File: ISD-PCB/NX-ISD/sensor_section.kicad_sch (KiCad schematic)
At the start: 27 parts, among them U10 BNO085, U11 PCA9306, U12 OPT3001DNPR, U3 MAX17048G_T10, U4 RV-3028-C7, U5 MAX30102, U6 BME690, Y2 32.768

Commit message: v1p3 - Isssues fixed
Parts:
- added R16, R17: 10k, Resistor_SMD:R_0402_1005Metric, symbol Device:R
- Y1: renamed from Y2; value 32.768 -> 32.768 kHz; Capacity (none) -> 12,5pF; ESR (none) -> 70 kOhms; Manufacterer part number (none) -> DH2032K768C5T1521011; Tolerance (none) -> ±20ppm
- renumbered C2 to C12, C1 to C13, C5 to C14, C18 to C15, C4 to C16, C7 to C17, C12 to C18, C30 to C19, C6 to C20, C29 to C21, C28 to C22, C27 to C23, R6 to R10, R23 to R11, R22 to R12, R18 to R13, R19 to R14, R24 to R15, R17 to R18, U12 to U10, U10 to U11, U4 to U12, U3 to U6, U6 to U7, U5 to U8, U11 to U9
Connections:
- net +3V3: now also U8.10 (VLED+), R16.1, R17.1
- net at U11.15 (ENV_SCL): now also R17.2
- net at U11.16 (ENV_SDA): now also R16.2
- no-connect marks 3 -> 1
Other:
- moved on the sheet: R18

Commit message: v1p3 - fixed
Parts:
- C14: value 100n -> 1u; footprint Capacitor_SMD:C_0402_1005Metric -> Capacitor_SMD:C_0603_1608Metric
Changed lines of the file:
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@@
 		)
 	)
+	(text "[0603]"
+		(exclude_from_sim no)
+		(at 31.242 176.53 0)
+		(effects
+			(font
+				(size 1.27 1.27)
+			)
+		)
+	)
 	(junction
 		(at 266.7 63.5)
@@
 		(dnp no)
 		(property "Reference" "C16"
-			(at 86.36 63.246 0)
+			(at 86.868 60.706 0)
 			(show_name no)
 			(do_not_autoplace no)
@@
 		)
 		(property "Value" "1u"
-			(at 86.868 66.04 0)
+			(at 88.138 65.786 0)
 			(show_name no)
 			(do_not_autoplace no)
@@
 		(dnp no)
 		(property "Reference" "C15"
-			(at 44.704 174.498 90)
+			(at 43.18 169.418 0)
 			(show_name no)
 			(do_not_autoplace no)
@@
 		)
 		(property "Value" "100n"
-			(at 51.816 174.752 90)
+			(at 42.926 175.006 0)
 			(show_name no)
 			(do_not_autoplace no)
@@
 		(dnp no)
 		(property "Reference" "C14"
-			(at 34.544 174.498 90)
+			(at 33.528 169.672 0)
 			(show_name no)
 			(do_not_autoplace no)
@@
 			)
 		)
-		(property "Value" "100n"
-			(at 41.656 174.752 90)
+		(property "Value" "1u"
+			(at 34.798 175.26 0)
 			(show_name no)
 			(do_not_autoplace no)
@@
 			)
 		)
-		(property "Footprint" "Capacitor_SMD:C_0402_1005Metric"
+		(property "Footprint" "Capacitor_SMD:C_0603_1608Metric"
 			(at 39.0652 176.53 0)
 			(hide yes)

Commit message: v1p3 - HRM Cap fix &more
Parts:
- removed C14: 1u, Capacitor_SMD:C_0603_1608Metric, symbol Device:C
- removed C15: 100n, Capacitor_SMD:C_0402_1005Metric, symbol Device:C
- added C30, C31: 100n, Capacitor_SMD:C_0402_1005Metric, symbol Device:C
- added C32: 4.7u, Capacitor_SMD:C_0603_1608Metric, symbol Device:C
- added C33: 10u, Capacitor_SMD:C_0603_1608Metric, symbol Device:C
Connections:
- net +1V8: now also C31.1, C32.1
- net +3V3: now also C30.1, C33.1
- net GND: now also C30.2, C31.2, C32.2, C33.2

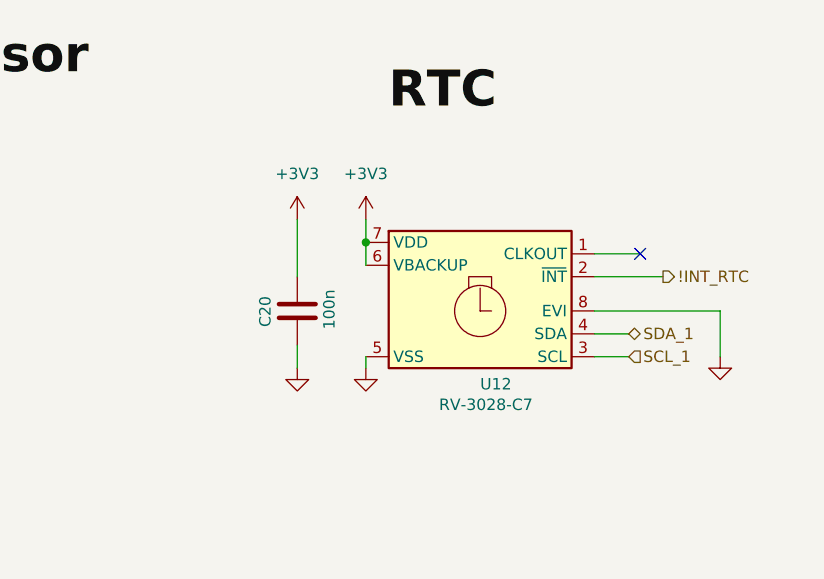
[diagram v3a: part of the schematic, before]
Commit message: v1p3 - RTC fix
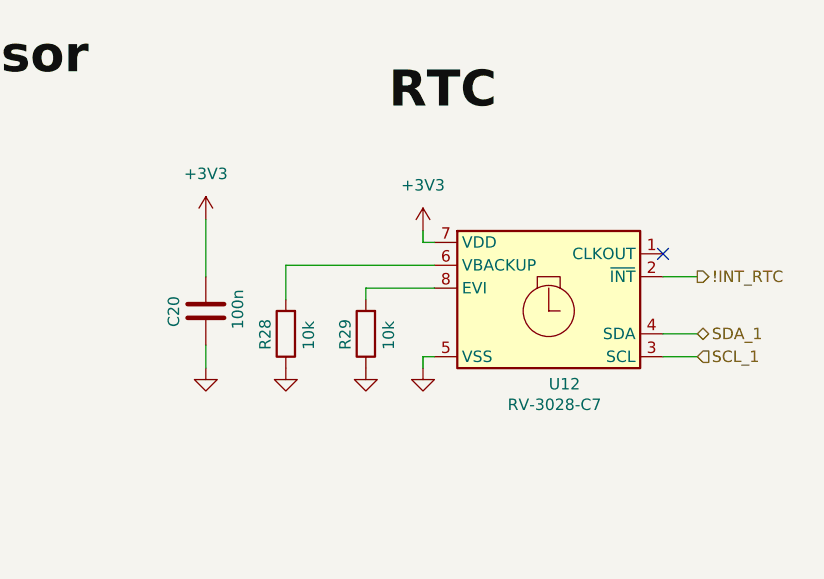
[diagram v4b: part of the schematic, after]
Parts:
- added R28, R29: 10k, Resistor_SMD:R_0402_1005Metric, symbol Device:R
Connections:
- net +3V3: no longer U12.6 (VBACKUP)
- net GND: now also R28.1, R29.1; no longer U12.8 (EVI)
- new net: R28.2, U12.6 (VBACKUP)
- new net: R29.2, U12.8 (EVI)
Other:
- moved on the sheet: C20, U12
